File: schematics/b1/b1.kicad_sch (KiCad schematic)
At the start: 37 parts, among them SW1 PWR_SW, U1 L7805, U2 AMS1117-3.3

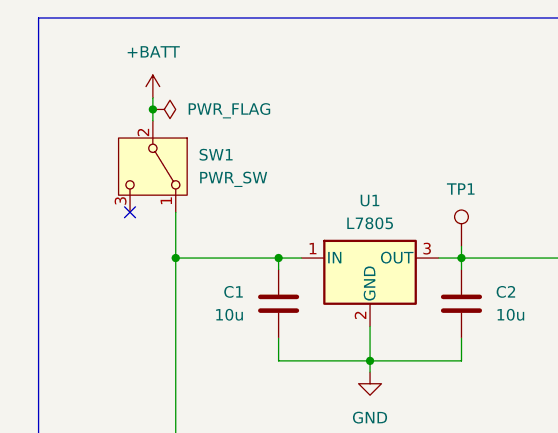
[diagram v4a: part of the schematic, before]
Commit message: Added terminal block for power in.
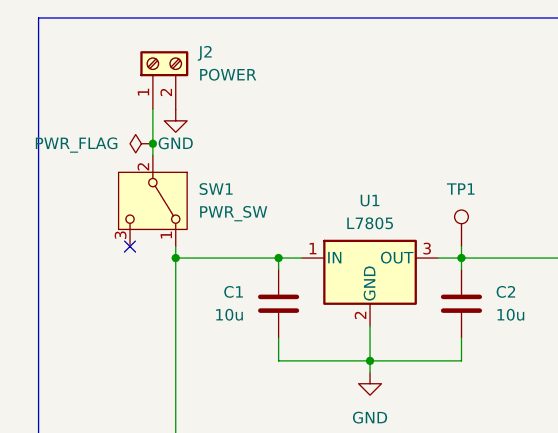
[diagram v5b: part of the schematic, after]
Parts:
- added J2: POWER, TerminalBlock:TerminalBlock_bornier-2_P5.08mm, symbol Connector:Screw_Terminal_01x02
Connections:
- net GND: now also J2.2 (Pin_2)
- net +BATT: no longer names the net of SW1.2 (B)
- net +BATT: now also J2.1 (Pin_1)
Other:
- moved on the sheet: SW1
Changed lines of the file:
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@@
   (junction (at 40.64 138.43) (diameter 0) (color 0 0 0 0)
   )
-  (junction (at 25.4 22.86) (diameter 0) (color 0 0 0 0)
+  (junction (at 25.4 26.67) (diameter 0) (color 0 0 0 0)
   )
   (junction (at 86.36 100.33) (diameter 0) (color 0 0 0 0)
@@
   (no_connect (at 177.8 39.37))
   (no_connect (at 177.8 46.99))
-  (no_connect (at 22.86 34.29))
+  (no_connect (at 22.86 38.1))
   (no_connect (at 177.8 87.63))
   (no_connect (at 177.8 85.09))
@@
     (stroke (width 0) (type default))
   )
-  (wire (pts (xy 25.4 21.59) (xy 25.4 22.86))
+  (wire (pts (xy 25.4 22.86) (xy 25.4 26.67))
     (stroke (width 0) (type default))
   )
@@
     (stroke (width 0) (type default))
   )
-  (wire (pts (xy 25.4 22.86) (xy 25.4 24.13))
+  (wire (pts (xy 25.4 26.67) (xy 25.4 27.94))
     (stroke (width 0) (type default))
   )
@@
     (stroke (width 0) (type default))
   )
-  (wire (pts (xy 27.94 34.29) (xy 27.94 39.37))
+  (wire (pts (xy 27.94 38.1) (xy 27.94 39.37))
     (stroke (width 0) (type default))
   )
@@
     )
   )
+  (symbol (lib_id "Connector:Screw_Terminal_01x02") (at 25.4 17.78 90) (unit 1)
+    (in_bom yes) (on_board yes) (dnp no)
+    (property "Reference" "J2" (at 30.48 16.51 90)
+      (effects (font (size 1.27 1.27)) (justify right))
+    )
+    (property "Value" "POWER" (at 30.48 19.05 90)
+      (effects (font (size 1.27 1.27)) (justify right))
+    )
+    (property "Footprint" "TerminalBlock:TerminalBlock_bornier-2_P5.08mm" (at 25.4 17.78 0)
+      (effects (font (size 1.27 1.27)) hide)
+    )
+    (property "Datasheet" "~" (at 25.4 17.78 0)
+      (effects (font (size 1.27 1.27)) hide)
+    )
+    (pin "2")
+    (pin "1")
+    (instances
+      (project "b1"
+        (path "/d6142fa5-2354-4512-9919-37616259c364"
+          (reference "J2") (unit 1)
+        )
+      )
+    )
+  )
   (symbol (lib_id "Connector:TestPoint") (at 85.09 176.53 270) (unit 1)
     (in_bom yes) (on_board yes) (dnp no)
@@
     )
   )
-  (symbol (lib_id "power:+BATT") (at 25.4 21.59 0) (unit 1)
-    (in_bom yes) (on_board yes) (dnp no) (fields_autoplaced)
-    (property "Reference" "#PWR01" (at 25.4 25.4 0)
-      (effects (font (size 1.27 1.27)) hide)
-    )
-    (property "Value" "+BATT" (at 25.4 16.51 0)
-      (effects (font (size 1.27 1.27)))
-    )
-    (property "Footprint" "" (at 25.4 21.59 0)
-      (effects (font (size 1.27 1.27)) hide)
-    )
-    (property "Datasheet" "" (at 25.4 21.59 0)
-      (effects (font (size 1.27 1.27)) hide)
-    )
-    (pin "1")
-    (instances
-      (project "b1"
-        (path "/d6142fa5-2354-4512-9919-37616259c364"
-          (reference "#PWR01") (unit 1)
-        )
-      )
-    )
-  )
   (symbol (lib_id "Device:C") (at 59.69 74.93 0) (unit 1)
     (in_bom yes) (on_board yes) (dnp no)
@@
         (path "/d6142fa5-2354-4512-9919-37616259c364"
           (reference "C10") (unit 1)
+        )
+      )
+    )
+  )
+  (symbol (lib_id "power:GND") (at 27.94 22.86 0) (unit 1)
+    (in_bom yes) (on_board yes) (dnp no)
+    (property "Reference" "#PWR01" (at 27.94 29.21 0)
+      (effects (font (size 1.27 1.27)) hide)
+    )
+    (property "Value" "GND" (at 27.94 26.67 0)
+      (effects (font (size 1.27 1.27)))
+    )
+    (property "Footprint" "" (at 27.94 22.86 0)
+      (effects (font (size 1.27 1.27)) hide)
+    )
+    (property "Datasheet" "" (at 27.94 22.86 0)
+      (effects (font (size 1.27 1.27)) hide)
+    )
+    (pin "1")
+    (instances
+      (project "b1"
+        (path "/d6142fa5-2354-4512-9919-37616259c364"
+          (reference "#PWR01") (unit 1)
         )
       )
@@
     )
   )
-  (symbol (lib_id "power:PWR_FLAG") (at 25.4 22.86 270) (mirror x) (unit 1)
-    (in_bom yes) (on_board yes) (dnp no)
-    (property "Reference" "#FLG01" (at 27.305 22.86 0)
-      (effects (font (size 1.27 1.27)) hide)
-    )
-    (property "Value" "PWR_FLAG" (at 29.21 22.86 90)
-      (effects (font (size 1.27 1.27)) (justify left))
-    )
-    (property "Footprint" "" (at 25.4 22.86 0)
-      (effects (font (size 1.27 1.27)) hide)
-    )
-    (property "Datasheet" "~" (at 25.4 22.86 0)
+  (symbol (lib_id "power:PWR_FLAG") (at 25.4 26.67 90) (unit 1)
+    (in_bom yes) (on_board yes) (dnp no)
+    (property "Reference" "#FLG01" (at 23.495 26.67 0)
+      (effects (font (size 1.27 1.27)) hide)
+    )
+    (property "Value" "PWR_FLAG" (at 21.59 26.67 90)
+      (effects (font (size 1.27 1.27)) (justify left))
+    )
+    (property "Footprint" "" (at 25.4 26.67 0)
+      (effects (font (size 1.27 1.27)) hide)
+    )
+    (property "Datasheet" "~" (at 25.4 26.67 0)
       (effects (font (size 1.27 1.27)) hide)
     )
@@
     )
   )
-  (symbol (lib_id "Switch:SW_SPDT") (at 25.4 29.21 270) (unit 1)
+  (symbol (lib_id "Switch:SW_SPDT") (at 25.4 33.02 270) (unit 1)
     (in_bom yes) (on_board yes) (dnp no) (fields_autoplaced)
-    (property "Reference" "SW1" (at 30.48 27.94 90)
-      (effects (font (size 1.27 1.27)) (justify left))
-    )
-    (property "Value" "PWR_SW" (at 30.48 30.48 90)
-      (effects (font (size 1.27 1.27)) (justify left))
-    )
-    (property "Footprint" "custom:SW_SPDT" (at 25.4 29.21 0)
-      (effects (font (size 1.27 1.27)) hide)
-    )
-    (property "Datasheet" "~" (at 17.78 29.21 0)
-      (effects (font (size 1.27 1.27)) hide)
-    )
+    (property "Reference" "SW1" (at 30.48 31.75 90)
+      (effects (font (size 1.27 1.27)) (justify left))
+    )
+    (property "Value" "PWR_SW" (at 30.48 34.29 90)
+      (effects (font (size 1.27 1.27)) (justify left))
+    )
+    (property "Footprint" "custom:SW_SPDT" (at 25.4 33.02 0)
+      (effects (font (size 1.27 1.27)) hide)
+    )
+    (property "Datasheet" "~" (at 17.78 33.02 0)
+      (effects (font (size 1.27 1.27)) hide)
+    )

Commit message: Routed some traces.
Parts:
- C10, C11, C12, C13, C3, C4, C5, C8, C9: footprint Capacitor_THT:CP_Radial_D8.0mm_P3.80mm -> Capacitor_THT:CP_Radial_D4.0mm_P2.00mm
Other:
- moved on the sheet: J2, SW1, TP4

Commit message: Routed traces.
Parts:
- removed C11, C12, C13, C3, C4: C, Capacitor_THT:CP_Radial_D4.0mm_P2.00mm, symbol Device:C_Polarized
- removed TP15, TP16, TP17, TP19, TP8: TestPoint, TestPoint:TestPoint_Loop_D2.50mm_Drill1.0mm, symbol Connector:TestPoint
- added H1, H2, H3, H4: MountingHole, MountingHole:MountingHole_2.2mm_M2, symbol Mechanical:MountingHole
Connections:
- net 3V3: now also C5.1
- net 5V: no longer C5.1
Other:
- moved on the sheet: C10, C5, C8, C9, JP1, JP2
